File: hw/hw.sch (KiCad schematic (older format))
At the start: 10 parts, among them U1 74LS299, U2 74LS138, U3 Z80CPU, U4 74LS161, U5 CY7C199, U6 74LS107, X1 CXO_DIP8

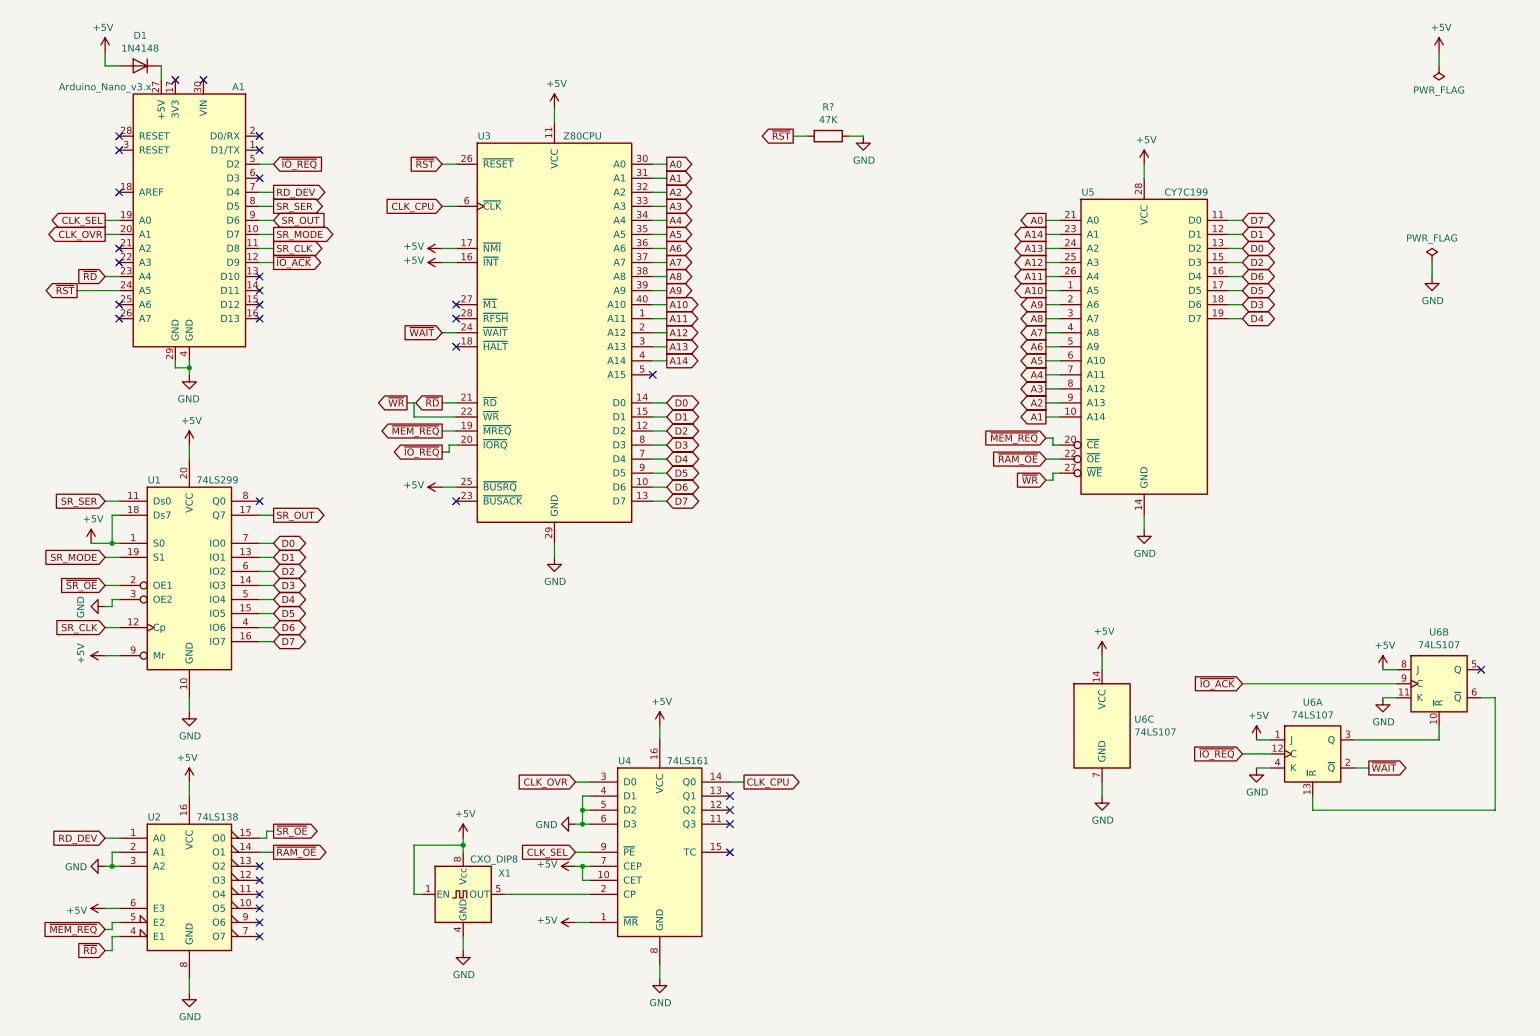
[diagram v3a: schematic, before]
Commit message: re-purpose IORQ as Arduino device output line and support read/write
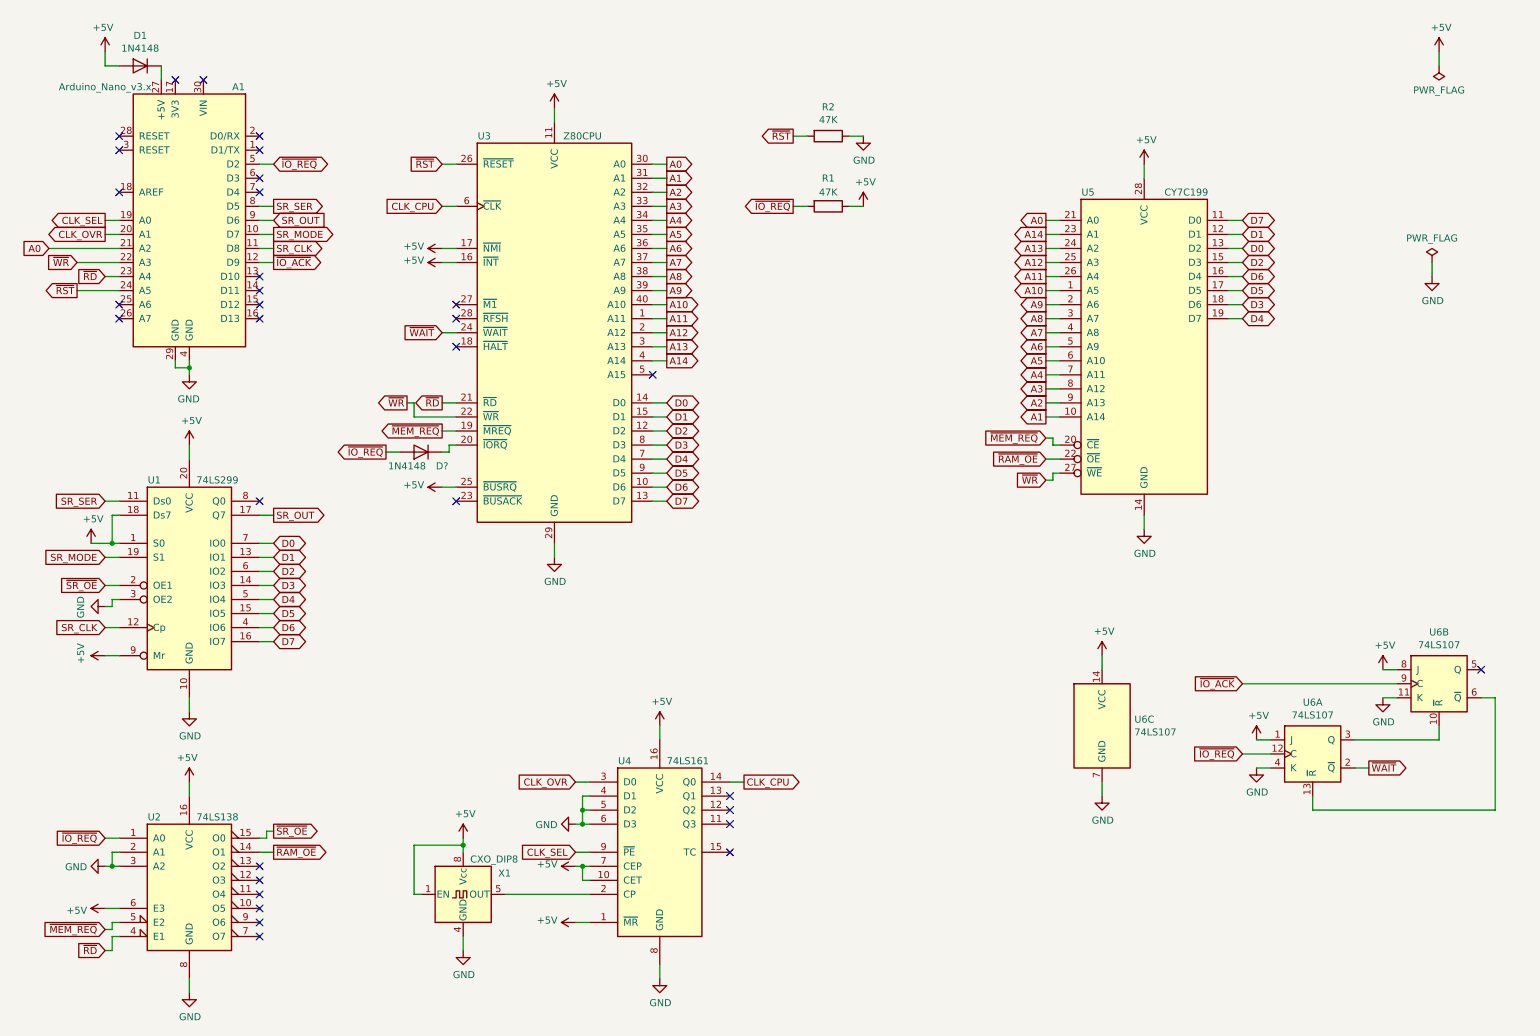
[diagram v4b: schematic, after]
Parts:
- added D?: 1N4148, Diode_THT:D_DO-35_SOD27_P7.62mm_Horizontal, symbol Diode:1N4148
- added R1: 47K, symbol Device:R
- gave numbers to parts that had none: 1
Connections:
- net +5V: now also R1.1
- net A0: now also A1.21 (A2)
- net ~IO_REQ: now also U2.1 (A0), D?.2 (A), R1.2; no longer U3.20 (~IORQ~)
- net ~WR: now also A1.22 (A3)
- net RD_DEV: no longer names the net of A1.7 (D4)
- net RD_DEV: no longer U2.1 (A0)
- new net: D?.1 (K), U3.20 (~IORQ~)
- no-connect marks 33 -> 32
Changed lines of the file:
@@
 Wire Wire Line
 	1100 2400 1200 2400
-NoConn ~ 1200 2200
-NoConn ~ 1200 2300
 NoConn ~ 1200 2600
 NoConn ~ 1200 2700
@@
 Wire Wire Line
 	1150 7000 1200 7000
-Text GLabel 1100 6400 0    50   Input ~ 0
-RD_DEV
 Text GLabel 1100 7200 0    50   Input ~ 0
 ~RD
@@
 Text GLabel 2300 2200 2    50   Output ~ 0
 SR_CLK
-Text GLabel 2300 1800 2    50   Output ~ 0
-RD_DEV
 Wire Wire Line
 	2300 2100 2200 2100
 Wire Wire Line
 	2200 2200 2300 2200
-Wire Wire Line
-	2300 1800 2200 1800
 Wire Wire Line
 	2200 1900 2300 1900
@@
 Wire Wire Line
 	8200 5100 8200 5200
-Text GLabel 3500 3650 0    50   Output ~ 0
+Text GLabel 3100 3650 0    50   Output ~ 0
 ~IO_REQ
 Wire Wire Line
@@
 	2300 2300 2200 2300
 NoConn ~ 2200 1700
-Text GLabel 2300 1600 2    50   Input ~ 0
+Text GLabel 2300 1600 2    50   BiDi ~ 0
 ~IO_REQ
 Wire Wire Line
@@
 ~RST
 $Comp
-L Device:R R?
+L Device:R R2
 U 1 1 5D4A0E06
 P 6250 1400
-F 0 "R?" V 6043 1400 50  0000 C CNN
+F 0 "R2" V 6043 1400 50  0000 C CNN
 F 1 "47K" V 6134 1400 50  0000 C CNN
 F 2 "" V 6180 1400 50  0001 C CNN
@@
 	6100 1400 6000 1400
 $Comp
-L power:GND #PWR?
+L power:GND #PWR013
 U 1 1 5D4B4F94
 P 6500 1400
-F 0 "#PWR?" H 6500 1150 50  0001 C CNN
+F 0 "#PWR013" H 6500 1150 50  0001 C CNN
 F 1 "GND" H 6505 1227 50  0000 C CNN
 F 2 "" H 6500 1400 50  0001 C CNN
@@
 	1    0    0    -1
 $EndComp
+$Comp
+L Device:R R1
+U 1 1 5D2BCE88
+P 6250 1900
+F 0 "R1" V 6050 1900 50  0000 C CNN
+F 1 "47K" V 6150 1900 50  0000 C CNN
+F 2 "" V 6180 1900 50  0001 C CNN
+F 3 "~" H 6250 1900 50  0001 C CNN
+	1    6250 1900
+	0    1    1    0
+$EndComp
+Wire Wire Line
+	3100 3650 3200 3650
+Text GLabel 1100 6400 0    50   Input ~ 0
+~IO_REQ
+Text GLabel 6000 1900 0    50   Output ~ 0
+~IO_REQ
+Wire Wire Line
+	6000 1900 6100 1900
+Wire Wire Line
+	6500 1900 6400 1900
+$Comp
+L power:+5V #PWR?
+U 1 1 5D2FB87F
+P 6500 1900
+F 0 "#PWR?" H 6500 1750 50  0001 C CNN
+F 1 "+5V" H 6515 2073 50  0000 C CNN
+F 2 "" H 6500 1900 50  0001 C CNN
+F 3 "" H 6500 1900 50  0001 C CNN
+	1    6500 1900
+	1    0    0    -1
+$EndComp
+$Comp
+L Diode:1N4148 D?
+U 1 1 5D2FBB80
+P 3350 3650
+F 0 "D?" H 3200 3750 50  0000 C CNN
+F 1 "1N4148" H 3450 3750 50  0000 C CNN
+F 2 "Diode_THT:D_DO-35_SOD27_P7.62mm_Horizontal" H 3350 3475 50  0001 C CNN
+F 3 "http://www.nxp.com/documents/data_sheet/1N4148_1N4448.pdf" H 3350 3650 50  0001 C CNN
+	1    3350 3650
+	-1   0    0    1
+$EndComp
+NoConn ~ 2200 1800
+Text GLabel 900  2300 0    50   Input ~ 0
+~WR
+Text GLabel 700  2200 0    50   Input ~ 0
+A0
+Wire Wire Line
+	900  2300 1200 2300
+Wire Wire Line
+	1200 2200 700  2200
 $EndSCHEMATC

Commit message: add output port
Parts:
- added U?: 74LS138, symbol 74xx:74LS138
- added U?: 74HCT574, symbol 74xx:74HCT574
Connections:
- net +5V: now also U?.16 (VCC), U?.20 (VCC), U?.6 (E3)
- net A0: now also U?.1 (A0)
- net A1: now also U?.2 (A1)
- net A2: now also U?.3 (A2)
- net D0: now also U?.2 (D0)
- net D1: now also U?.3 (D1)
- net D2: now also U?.4 (D2)
- net D3: now also U?.5 (D3)
- net D4: now also U?.6 (D4)
- net D5: now also U?.7 (D5)
- net D6: now also U?.8 (D6)
- net D7: now also U?.9 (D7)
- net GND: now also U?.1 (OE), U?.10 (GND), U?.8 (GND)
- net ~IO_REQ: now also U?.5 (E2)
- net ~WR: now also U?.4 (E1)
- new net ~PORTA_WR: U?.11 (Cp), U?.7 (O7)
- no-connect marks 32 -> 39
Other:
- moved on the sheet: R1, R2, U5
